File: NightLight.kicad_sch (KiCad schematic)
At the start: 17 parts, among them U1 magnetic-charger, U2 rdm-6300, U3 TP4056, U4 ESP32-WROOM-32

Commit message: Add lots of ocmponents
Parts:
- added C1: 22u, Capacitor_THT:CP_Radial_D5.0mm_P2.50mm, symbol Device:C_Polarized
- added J1: Conn_01x02, Connector_PinHeader_2.54mm:PinHeader_1x02_P2.54mm_Vertical, symbol Connector_Generic:Conn_01x02
- added J2: Micro_SD_Card, sd-card:sd-card, symbol Connector:Micro_SD_Card
- added LS1: Speaker, symbol Device:Speaker
- added U5: AMS1117-3.3, Package_TO_SOT_SMD:SOT-223-3_TabPin2, symbol Regulator_Linear:AMS1117-3.3
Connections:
- net +3V3: now also C1.1, J2.4 (VDD), U5.2 (VO); no longer U3.3 (O+)
- net CS: now also J2.2 (DAT3/CD)
- net GND: now also C1.2, J2.6 (VSS), J2.9 (SHIELD), LS1.1, U5.1 (GND)
- net MISO: now also J2.7 (DAT0)
- net MOSI: now also J2.3 (CMD)
- net SCK: now also J2.5 (CLK)
- net DAC1: now reaches U4.10 (IO25)
- net DAC1: now also LS1.2
- net DAC2: now reaches U4.11 (IO26)
- net TOUCH3: now reaches U4.12 (IO27)
- net TOUCH1: now reaches U4.8 (IO32)
- net TOUCH2: now reaches U4.9 (IO33)
- net at U2.6 (ANT): now also J1.1 (Pin_1)
- net at U2.7 (ANT): now also J1.2 (Pin_2)
- new net +4V: U3.3 (O+), U5.3 (VI)
- no-connect marks 5 -> 4
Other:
- note added: "TODO: - Test the SDCard setup with 2mm pitch things - Test the DAC setup"
- moved on the sheet: D1, D2, D3, D4, D5, D6, D7, H1, H2, R1, R2, R3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

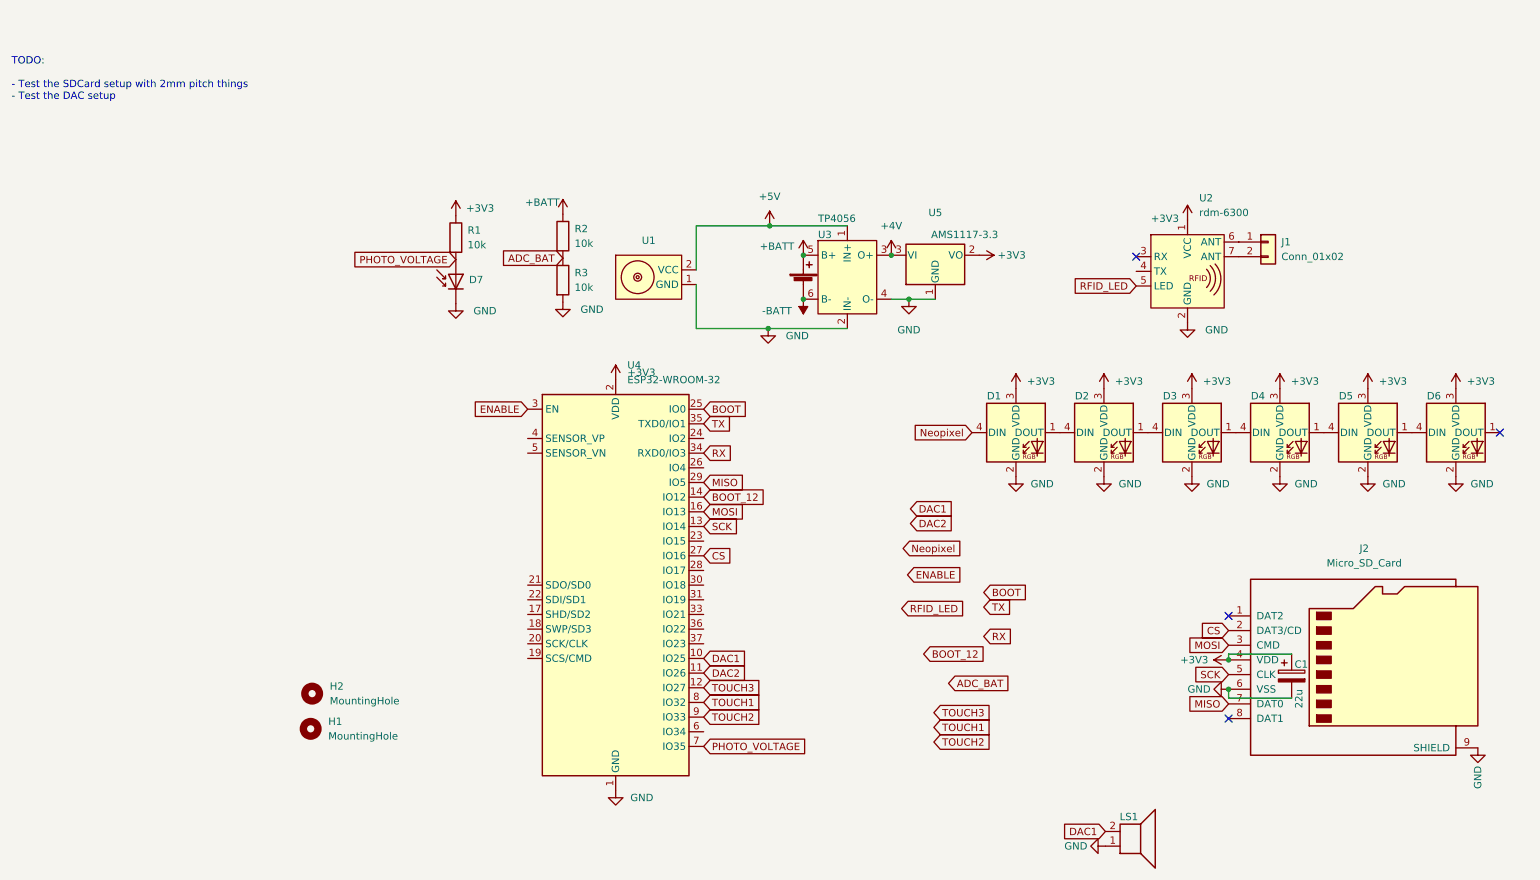
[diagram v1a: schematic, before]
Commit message: Add button and update the magnetic charger
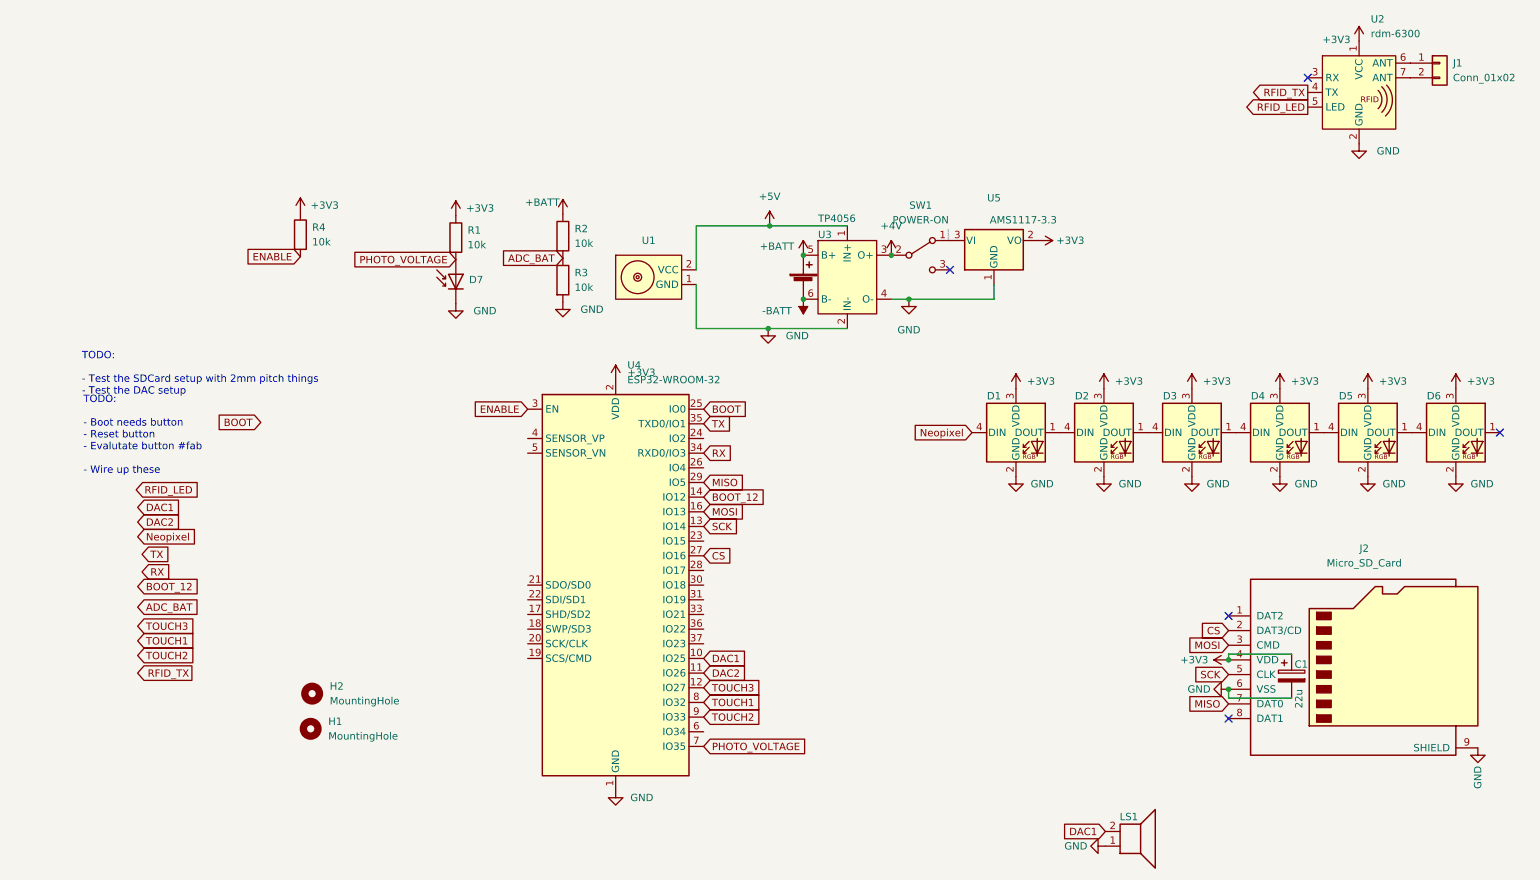
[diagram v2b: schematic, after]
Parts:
- added R4: 10k, Resistor_THT:R_Axial_DIN0204_L3.6mm_D1.6mm_P5.08mm_Horizontal, symbol Device:R
- added SW1: POWER-ON, Button_Switch_SMD:SW_SPDT_CK-JS102011SAQN, symbol Switch:SW_SPDT
- U5: footprint Package_TO_SOT_SMD:SOT-223-3_TabPin2 -> Package_TO_SOT_SMD:TO-252-2
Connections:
- net +3V3: now also R4.1
- net +4V: now also SW1.2 (B); no longer U5.3 (VI)
- net ENABLE: now also R4.2
- net RFID_TX: now reaches U2.4 (TX)
- new net +4V_Switched: SW1.1 (A), U5.3 (VI)
- no-connect marks 4 -> 5
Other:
- note added: "TODO: - Boot needs button - Reset button - Evalutate button #fab - Wire up these"
- moved on the sheet: J1, U2, U5

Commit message: Updates from card board prototype
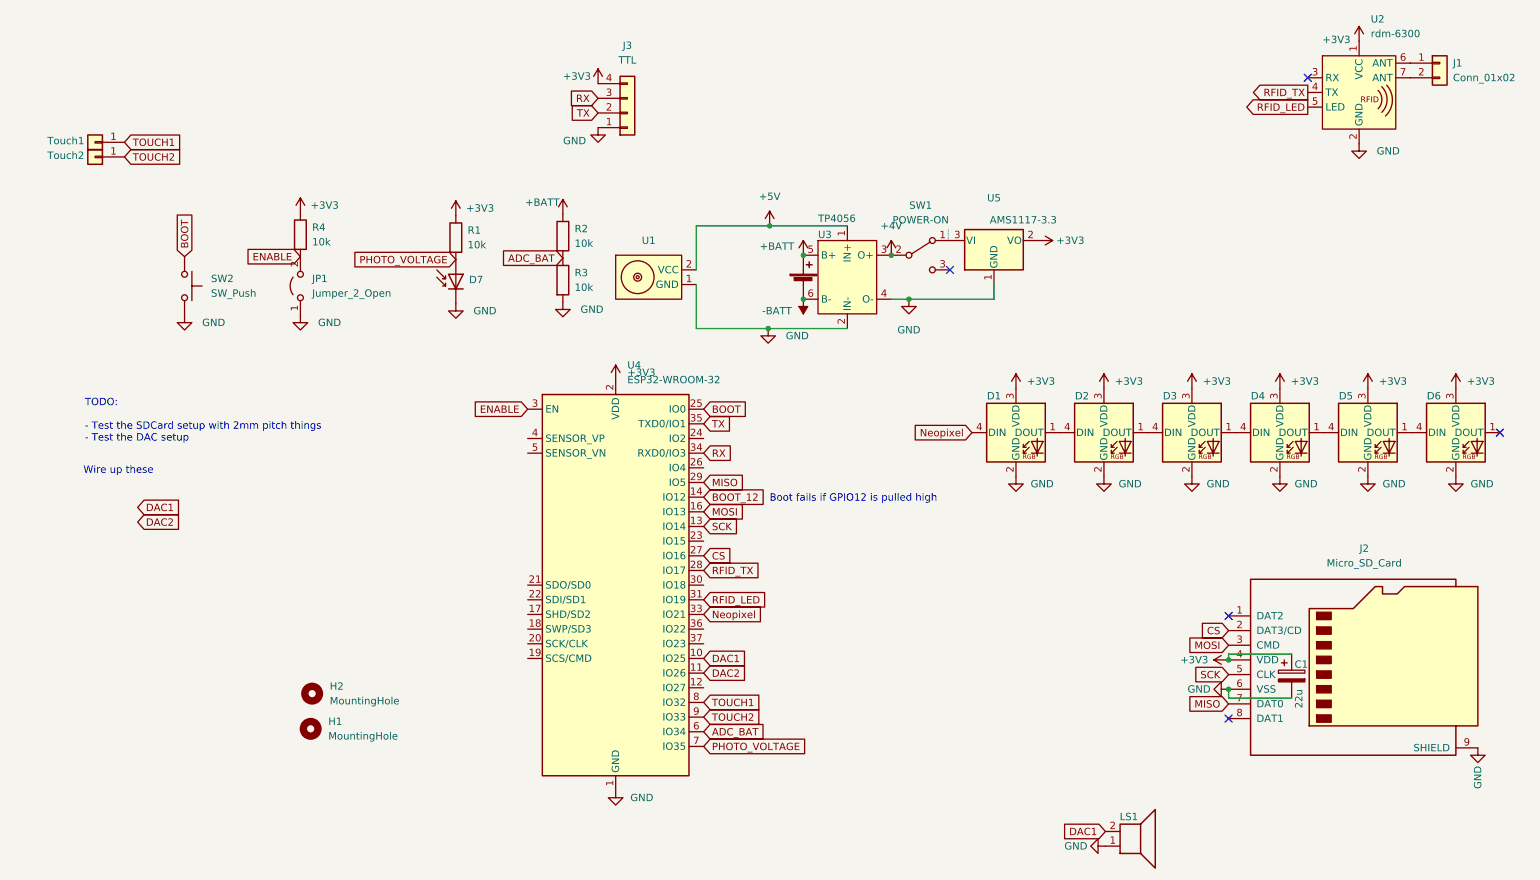
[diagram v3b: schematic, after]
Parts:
- added J3: TTL, Connector_PinHeader_2.54mm:PinHeader_1x04_P2.54mm_Vertical, symbol Connector_Generic:Conn_01x04
- added J5: Touch1, Connector_PinHeader_2.54mm:PinHeader_1x01_P2.54mm_Vertical, symbol Connector_Generic:Conn_01x01
- added J6: Touch2, Connector_PinHeader_2.54mm:PinHeader_1x01_P2.54mm_Vertical, symbol Connector_Generic:Conn_01x01
- added JP1: Jumper_2_Open, Connector_PinHeader_2.54mm:PinHeader_1x02_P2.54mm_Vertical, symbol Jumper:Jumper_2_Open
- added SW2: SW_Push, Button_Switch_THT:SW_PUSH_6mm_H4.3mm, symbol Switch:SW_Push
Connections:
- net +3V3: now also J3.4 (Pin_4)
- net ADC_BAT: now also U4.6 (IO34)
- net BOOT: now also SW2.1
- net ENABLE: now also JP1.2 (B)
- net GND: now also J3.1 (Pin_1), JP1.1 (A), SW2.2
- net Neopixel: now also U4.33 (IO21)
- net RFID_LED: now also U4.31 (IO19)
- net RFID_TX: now also U4.28 (IO17)
- net RX: now also J3.3 (Pin_3)
- net TOUCH1: now also J5.1 (Pin_1)
- net TOUCH2: now also J6.1 (Pin_1)
- net TX: now also J3.2 (Pin_2)
- net TOUCH3: no longer names the net of U4.12 (IO27)
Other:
- note added: "Boot fails if GPIO12 is pulled high"
- note added: "Wire up these"
- note removed: "TODO: - Boot needs button - Reset button - Evalutate button #fab - Wire up these"

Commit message: Add a speaker outlet
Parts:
- LS1: footprint (none) -> Connector_PinHeader_2.54mm:PinHeader_1x02_P2.54mm_Vertical
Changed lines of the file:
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@@
       (effects (font (size 1.27 1.27)) hide)
     )
-    (property "Footprint" "" (id 2) (at 214.63 152.654 0)
+    (property "Footprint" "Connector_PinHeader_2.54mm:PinHeader_1x02_P2.54mm_Vertical" (id 2) (at 214.63 152.654 0)
       (effects (font (size 1.27 1.27)) hide)
     )
@@
     )
     (path "/593e3d3f-e5a7-4a9a-b213-3f90d771c103"
-      (reference "LS1") (unit 1) (value "Speaker") (footprint "")
+      (reference "LS1") (unit 1) (value "Speaker") (footprint "Connector_PinHeader_2.54mm:PinHeader_1x02_P2.54mm_Vertical")
     )
     (path "/e508d49e-3f8e-4efa-b7d5-ab207a802581"
